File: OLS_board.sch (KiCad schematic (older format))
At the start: 18 parts, among them J1 CONN_3X2, J2 CONN_3X2, P1 CONN_9, P2 CONN_9, P3 CONN_9, P4 CONN_9, P9 CONN_4, SW1 DIPS_08, SW2 DIPS_08, SW3 DIPS_08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

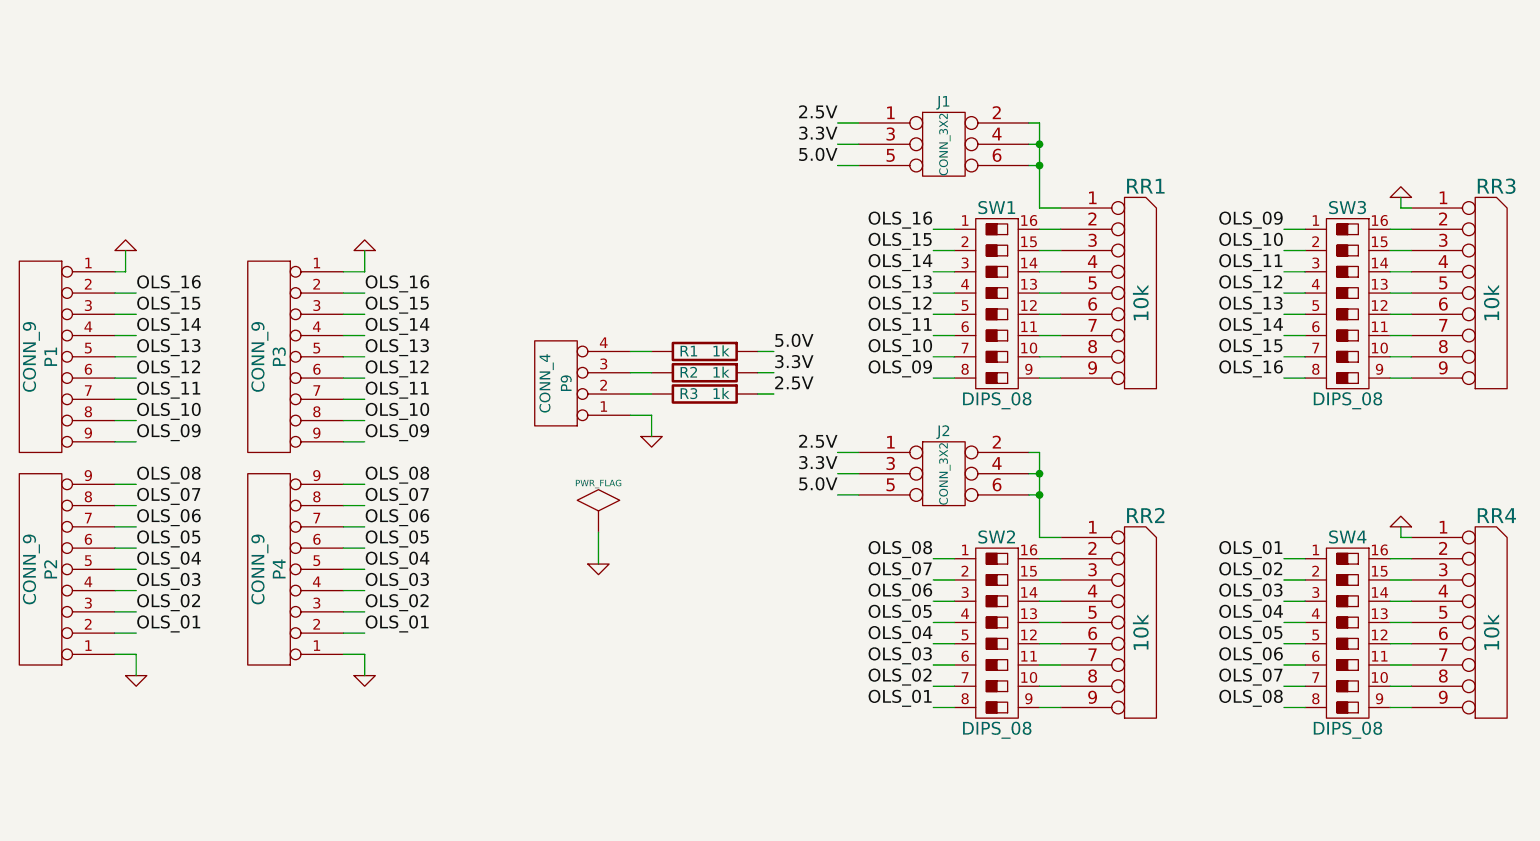
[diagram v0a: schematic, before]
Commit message: Small schematic tweaks (just readability, not functionality).
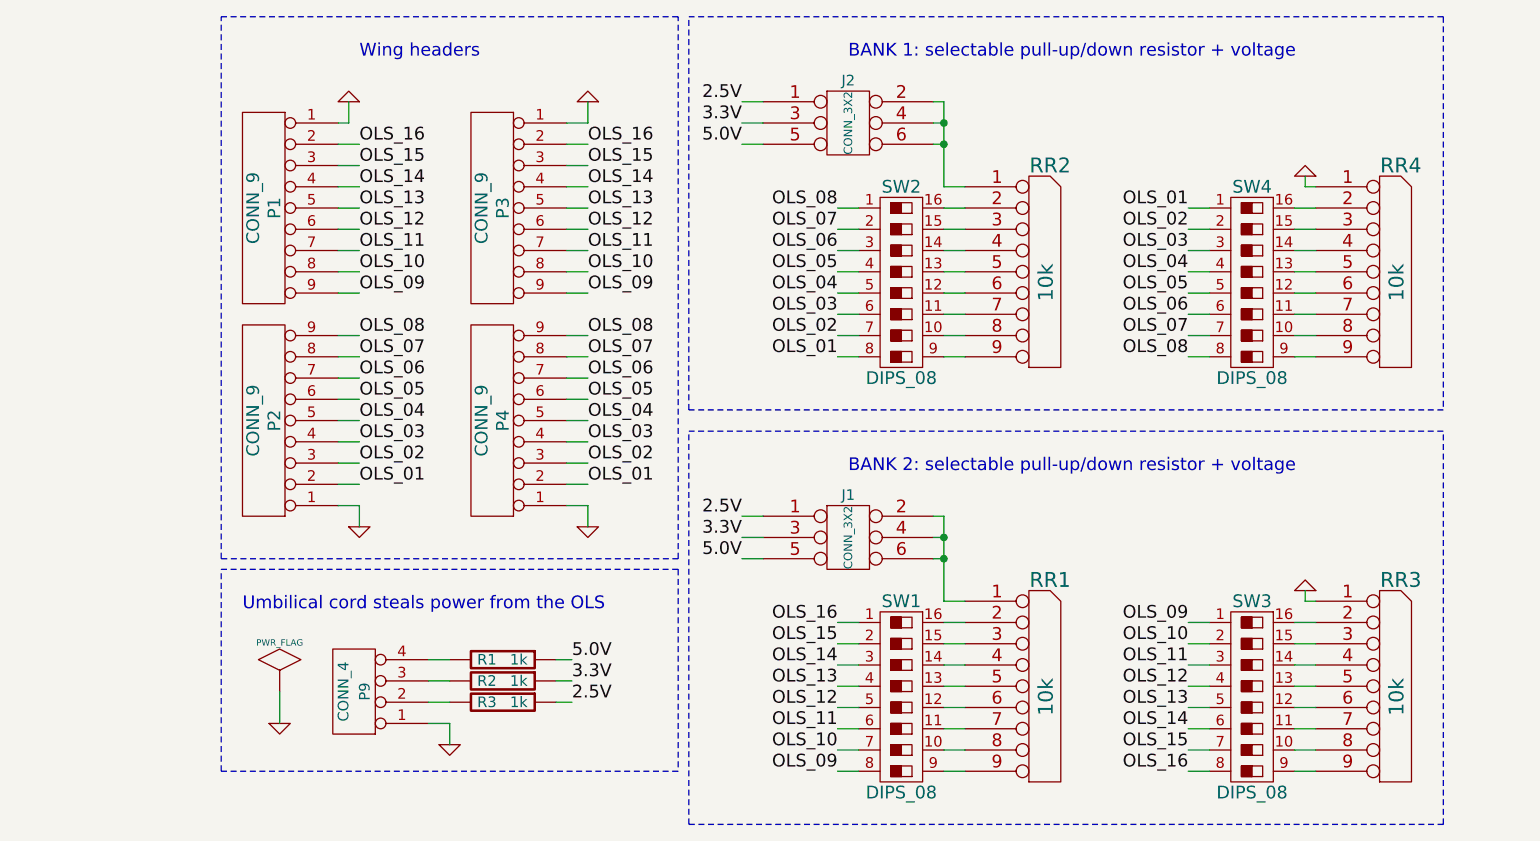
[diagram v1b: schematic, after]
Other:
- note added: "BANK 1: selectable pull-up/down resistor + voltage"
- note added: "BANK 2: selectable pull-up/down resistor + voltage"
- note added: "Umbilical cord steals power from the OLS"
- note added: "Wing headers"
- moved on the sheet: J1, J2, P1, P2, P3, P4, P9, R1, R2, R3, RR1, RR2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
